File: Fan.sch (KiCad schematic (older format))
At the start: 0 parts

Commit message: Understanding the Current/Fan Driver Module
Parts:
- added Q?: MOSFET_N, symbol MOSFET_N
- added R? (x5): R, symbol R
- added RV?: POT, symbol POT
- added U?: LM324, symbol LM324
- added U?: MCP4922-E/SL, SO14, symbol MCP4922-E/SL
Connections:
- net Fan_In: now also R?.2, R?.2
- net Power+: now also Q?.S
- new net: Q?.G, U?.1
- new net: R?.2, R?.2, RV?.3, U?.3 (+)
- new net: R?.1, U?.14 (VoutA)
- new net: R?.1, U?.9 (~SHDN~)
- new net +12V: Q?.D, R?.1, U?.4 (V+)
- new net -12V: U?.11 (V-)
- new net AGND: R?.2, RV?.1
- new net CS_N: U?.3 (~CS~)
- new net Current_Measure: R?.1, U?.2 (-)
- new net MOSI: U?.5 (SDI)
- new net SCLK: U?.4 (SCK)
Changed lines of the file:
@@
 LIBS:contrib
 LIBS:valves
+LIBS:MyComponents
 LIBS:BenchBuddy-cache
 EELAYER 24 0
@@
 Comment4 ""
 $EndDescr
-Text HLabel 9250 2250 2    60   Output ~ 0
+Text HLabel 9500 2750 2    60   Output ~ 0
 Power+
-Text HLabel 9250 2550 2    60   Input ~ 0
+Text HLabel 9500 3050 2    60   Input ~ 0
 Power-
-Text HLabel 9250 2900 2    60   Input ~ 0
+Text HLabel 10250 5150 2    60   Input ~ 0
 Tach_In
-Text HLabel 1850 2050 0    60   Output ~ 0
+Text HLabel 1700 5150 0    60   Output ~ 0
 Tach_Out
-Text HLabel 1850 2350 0    60   Input ~ 0
+Text HLabel 1750 3350 0    60   Input ~ 0
 Fan_In
+Wire Wire Line
+	1700 5150 10250 5150
+$Comp
+L LM324 U?
+U 1 1 52F15AC1
+P 6750 2200
+F 0 "U?" H 6800 2400 60  0000 C CNN
+F 1 "LM324" H 6900 2000 50  0000 C CNN
+F 2 "" H 6750 2200 60  0000 C CNN
+F 3 "" H 6750 2200 60  0000 C CNN
+	1    6750 2200
+	1    0    0    -1
+$EndComp
+$Comp
+L MOSFET_N Q?
+U 1 1 52F15ADF
+P 8100 2200
+F 0 "Q?" H 8110 2370 60  0000 R CNN
+F 1 "MOSFET_N" H 8110 2050 60  0000 R CNN
+F 2 "" H 8100 2200 60  0000 C CNN
+F 3 "" H 8100 2200 60  0000 C CNN
+	1    8100 2200
+	1    0    0    -1
+$EndComp
+$Comp
+L +12V #PWR?
+U 1 1 52F15AF3
+P 8200 1750
+F 0 "#PWR?" H 8200 1700 20  0001 C CNN
+F 1 "+12V" H 8200 1850 30  0000 C CNN
+F 2 "" H 8200 1750 60  0000 C CNN
+F 3 "" H 8200 1750 60  0000 C CNN
+	1    8200 1750
+	1    0    0    -1
+$EndComp
+Wire Wire Line
+	7900 2200 7250 2200
+Wire Wire Line
+	8200 2400 8200 2750
+Wire Wire Line
+	8200 2750 9500 2750
+Wire Wire Line
+	6000 3050 9500 3050
+Wire Wire Line
+	8200 3050 8200 3850
+$Comp
+L R R?
+U 1 1 52F15B2A
+P 8200 4100
+F 0 "R?" V 8280 4100 40  0000 C CNN
+F 1 "R" V 8207 4101 40  0000 C CNN
+F 2 "" V 8130 4100 30  0000 C CNN
+F 3 "" H 8200 4100 30  0000 C CNN
+	1    8200 4100
+	1    0    0    -1
+$EndComp
+$Comp
+L AGND #PWR?
+U 1 1 52F15B46
+P 8200 4700
+F 0 "#PWR?" H 8200 4700 40  0001 C CNN
+F 1 "AGND" H 8200 4630 50  0000 C CNN
+F 2 "" H 8200 4700 60  0000 C CNN
+F 3 "" H 8200 4700 60  0000 C CNN
+	1    8200 4700
+	1    0    0    -1
+$EndComp
+Wire Wire Line
+	8200 4350 8200 4700
+Wire Wire Line
+	6000 3050 6000 2300
+Wire Wire Line
+	6000 2300 6250 2300
+Connection ~ 8200 3050
+Wire Wire Line
+	8200 2000 8200 1750
+$Comp
+L +12V #PWR?
+U 1 1 52F15B77
+P 6650 1700
+F 0 "#PWR?" H 6650 1650 20  0001 C CNN
+F 1 "+12V" H 6650 1800 30  0000 C CNN
+F 2 "" H 6650 1700 60  0000 C CNN
+F 3 "" H 6650 1700 60  0000 C CNN
+	1    6650 1700
+	1    0    0    -1
+$EndComp
+Wire Wire Line
+	6650 1700 6650 1800
+$Comp
+L -12V #PWR?
+U 1 1 52F15B91
+P 6650 2700
+F 0 "#PWR?" H 6650 2830 20  0001 C CNN
+F 1 "-12V" H 6650 2800 30  0000 C CNN
+F 2 "" H 6650 2700 60  0000 C CNN
+F 3 "" H 6650 2700 60  0000 C CNN
+	1    6650 2700
+	-1   0    0    1
+$EndComp
+Wire Wire Line
+	6650 2700 6650 2600
+$Comp
+L R R?
+U 1 1 52F15BC1
+P 5400 1700
+F 0 "R?" V 5480 1700 40  0000 C CNN
+F 1 "R" V 5407 1701 40  0000 C CNN
+F 2 "" V 5330 1700 30  0000 C CNN
+F 3 "" H 5400 1700 30  0000 C CNN
+	1    5400 1700
+	1    0    0    -1
+$EndComp
+$Comp
+L +12V #PWR?
+U 1 1 52F15BCC
+P 5400 1350
+F 0 "#PWR?" H 5400 1300 20  0001 C CNN
+F 1 "+12V" H 5400 1450 30  0000 C CNN
+F 2 "" H 5400 1350 60  0000 C CNN
+F 3 "" H 5400 1350 60  0000 C CNN
+	1    5400 1350
+	1    0    0    -1
+$EndComp
+Wire Wire Line
+	5400 1350 5400 1450
+$Comp
+L POT RV?
+U 1 1 52F15C37
+P 5400 2550
+F 0 "RV?" H 5400 2450 50  0000 C CNN
+F 1 "POT" H 5400 2550 50  0000 C CNN
+F 2 "" H 5400 2550 60  0000 C CNN
+F 3 "" H 5400 2550 60  0000 C CNN
+	1    5400 2550
+	0    -1   -1   0
+$EndComp
+$Comp
+L AGND #PWR?
+U 1 1 52F15C5C
+P 5400 3000
+F 0 "#PWR?" H 5400 3000 40  0001 C CNN
+F 1 "AGND" H 5400 2930 50  0000 C CNN
+F 2 "" H 5400 3000 60  0000 C CNN
+F 3 "" H 5400 3000 60  0000 C CNN
+	1    5400 3000
+	1    0    0    -1
+$EndComp
+Wire Wire Line
+	5400 3000 5400 2800
+Wire Wire Line
+	5400 1950 5400 2300
+Wire Wire Line
+	4300 2100 6250 2100
+Connection ~ 5400 2100
+Text HLabel 1900 1850 0    60   Output ~ 0
+MISO
+Text HLabel 1900 2050 0    60   Input ~ 0
+MOSI
+Text HLabel 1900 2150 0    60   Input ~ 0
+SCLK
+Text HLabel 1900 2250 0    60   Input ~ 0
+CS_N
+Text HLabel 1750 3700 0    60   Output ~ 0
+Current_Measure
+$Comp
+L R R?
+U 1 1 52F15DC9
+P 5700 2550
+F 0 "R?" V 5780 2550 40  0000 C CNN
+F 1 "R" V 5707 2551 40  0000 C CNN
+F 2 "" V 5630 2550 30  0000 C CNN
+F 3 "" H 5700 2550 30  0000 C CNN
+	1    5700 2550
+	1    0    0    -1
+$EndComp
+Wire Wire Line
+	1750 3700 8200 3700
+Connection ~ 8200 3700
+Wire Wire Line
+	5700 3350 5700 2800
+Wire Wire Line
+	1750 3350 5700 3350
+$Comp
+L R R?
+U 1 1 52F15E21
+P 4050 2100
+F 0 "R?" V 4130 2100 40  0000 C CNN
+F 1 "R" V 4057 2101 40  0000 C CNN
+F 2 "" V 3980 2100 30  0000 C CNN
+F 3 "" H 4050 2100 30  0000 C CNN
+	1    4050 2100
+	0    -1   -1   0
+$EndComp
+Wire Wire Line
+	1900 2050 2200 2050
+Wire Wire Line
+	1900 2150 2200 2150
+Wire Wire Line
+	1900 2250 2200 2250
+$Comp
+L R R?
+U 1 1 52F15EBA
+P 2200 2800
+F 0 "R?" V 2280 2800 40  0000 C CNN
+F 1 "R" V 2207 2801 40  0000 C CNN
+F 2 "" V 2130 2800 30  0000 C CNN
+F 3 "" H 2200 2800 30  0000 C CNN
+	1    2200 2800
+	1    0    0    -1
+$EndComp
+Wire Wire Line
+	2200 3050 2200 3350
+Connection ~ 2200 3350
+$Comp
+L MCP4922-E/SL U?
+U 1 1 52F15F05
+P 2750 2250
+F 0 "U?" H 2900 2650 40  0000 L BNN
+F 1 "MCP4922-E/SL" H 2900 2600 40  0000 L BNN
+F 2 "SO14" H 2750 2250 30  0000 C CIN
+F 3 "" H 2750 2250 60  0000 C CNN
+	1    2750 2250
+	1    0    0    -1
+$EndComp
+Wire Wire Line
+	3300 2100 3800 2100
+Wire Wire Line
+	2200 2450 2200 2550
 $EndSCHEMATC

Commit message: Understanding the Arduino Module
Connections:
- net Current_Measure renamed CURR_MEAS
- net Fan_In renamed FAN_EN_N
- net Power+ renamed FAN_OUT+
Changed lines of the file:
@@
 LIBS:valves
 LIBS:MyComponents
+LIBS:arduino_shieldsNCL
 LIBS:BenchBuddy-cache
 EELAYER 24 0
@@
 $Descr A4 11693 8268
 encoding utf-8
-Sheet 8 9
+Sheet 9 9
 Title ""
 Date ""
@@
 $EndDescr
 Text HLabel 9500 2750 2    60   Output ~ 0
-Power+
-Text HLabel 9500 3050 2    60   Input ~ 0
-Power-
+FAN_OUT+
+Text HLabel 9500 3050 2    60   Output ~ 0
+FAN_OUT-
 Text HLabel 10250 5150 2    60   Input ~ 0
-Tach_In
+TACH_IN
 Text HLabel 1700 5150 0    60   Output ~ 0
-Tach_Out
+TACH_MEAS
 Text HLabel 1750 3350 0    60   Input ~ 0
-Fan_In
+FAN_EN_N
 Wire Wire Line
 	1700 5150 10250 5150
@@
 CS_N
 Text HLabel 1750 3700 0    60   Output ~ 0
-Current_Measure
+CURR_MEAS
 $Comp
 L R R?

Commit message: Revisting the Current/Fan Module
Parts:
- removed R? (x3): R, symbol R
- removed RV?: POT, symbol POT
- added D?: DIODE, symbol DIODE
- added Q? (x2): MOSFET_N, symbol MOSFET_N
- added TH?: THERMISTOR, symbol THERMISTOR
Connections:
- net +12V: no longer Q?.D
- net AGND: now also Q?.S, Q?.S
- net CURR_MEAS: now also Q?.S, Q?.D
- net FAN_OUT+: now also D?.2 (K), TH?.2; no longer Q?.S
- net at R?.2, U?.3 (+): now also Q?.D
- new net +12C: TH?.1
- new net FAN_MODE: Q?.G
- new net FAN_OUT-: D?.1 (A), Q?.D
- new net FAN_PWM: Q?.G
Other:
- moved on the sheet: Q?, R?, U?, U?A

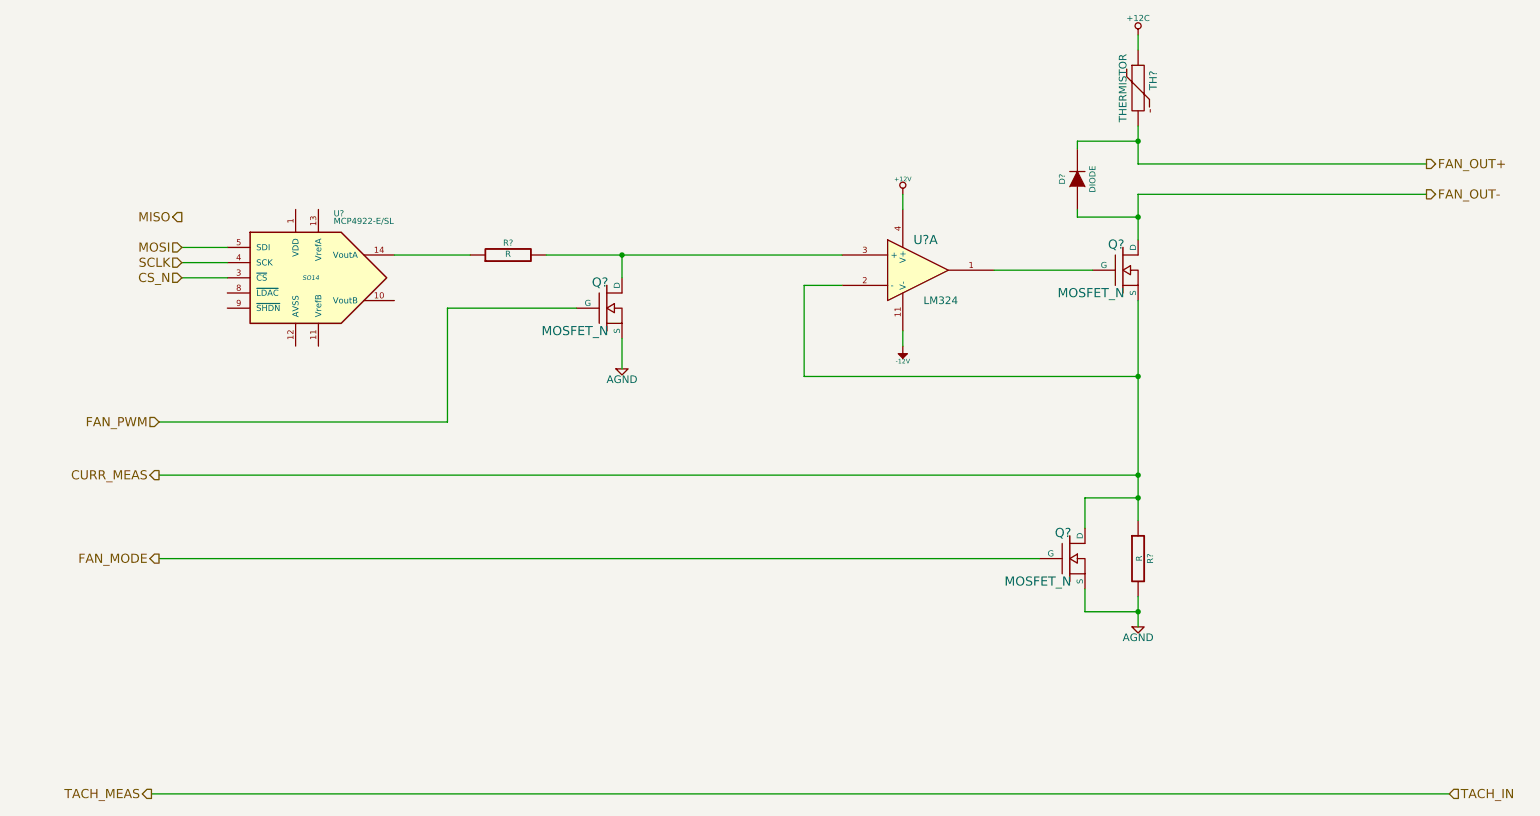
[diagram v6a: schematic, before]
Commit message: Associating and Placing the Relay Module
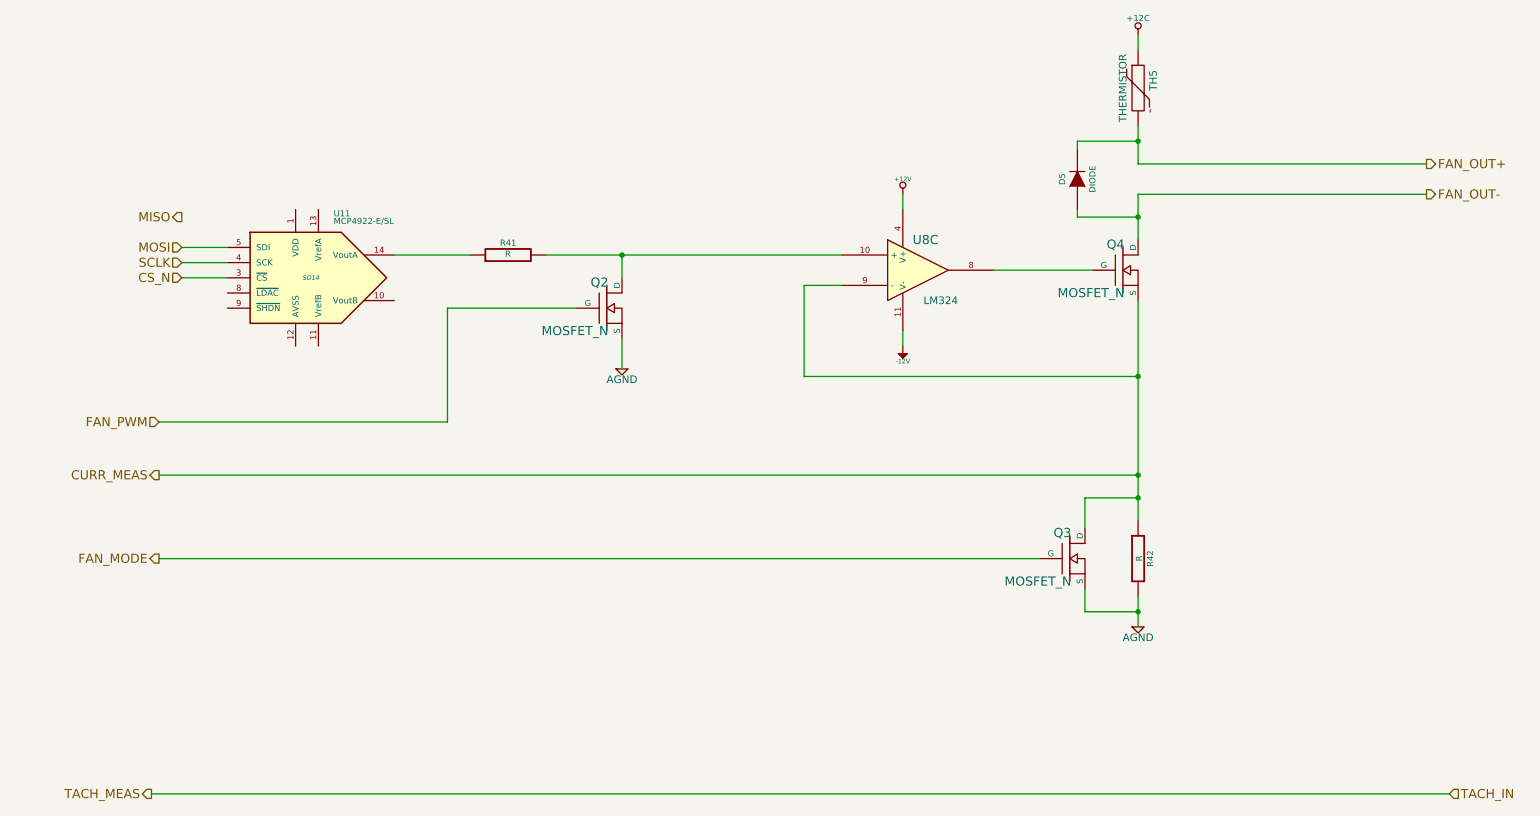
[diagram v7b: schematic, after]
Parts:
- gave numbers to parts that had none: 9
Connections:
- net CURR_MEAS: now also U8.9 (-); no longer U8.2 (-)
- net at Q4.G: now also U8.8; no longer U8.1
- net at Q2.D, R41.2: now also U8.10 (+); no longer U8.3 (+)
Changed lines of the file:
@@
 FAN_PWM
 $Comp
-L LM324 U?
-U 1 1 52F15AC1
+L LM324 U8
+U 3 1 52F15AC1
 P 6750 2350
-F 0 "U?" H 6800 2550 60  0000 C CNN
+F 0 "U8" H 6800 2550 60  0000 C CNN
 F 1 "LM324" H 6900 2150 50  0000 C CNN
 F 2 "" H 6750 2350 60  0000 C CNN
 F 3 "" H 6750 2350 60  0000 C CNN
-	1    6750 2350
-	1    0    0    -1
-$EndComp
-$Comp
-L MOSFET_N Q?
+	3    6750 2350
+	1    0    0    -1
+$EndComp
+$Comp
+L MOSFET_N Q4
 U 1 1 52F15ADF
 P 8100 2350
-F 0 "Q?" H 8110 2520 60  0000 R CNN
+F 0 "Q4" H 8110 2520 60  0000 R CNN
 F 1 "MOSFET_N" H 8110 2200 60  0000 R CNN
 F 2 "" H 8100 2350 60  0000 C CNN
@@
 $EndComp
 $Comp
-L R R?
+L R R42
 U 1 1 52F15B2A
 P 8200 4250
-F 0 "R?" V 8280 4250 40  0000 C CNN
+F 0 "R42" V 8280 4250 40  0000 C CNN
 F 1 "R" V 8207 4251 40  0000 C CNN
 F 2 "" V 8130 4250 30  0000 C CNN
@@
 $EndComp
 $Comp
-L AGND #PWR?
+L AGND #PWR051
 U 1 1 52F15B46
 P 8200 4700
-F 0 "#PWR?" H 8200 4700 40  0001 C CNN
+F 0 "#PWR051" H 8200 4700 40  0001 C CNN
 F 1 "AGND" H 8200 4630 50  0000 C CNN
 F 2 "" H 8200 4700 60  0000 C CNN
@@
 $EndComp
 $Comp
-L +12V #PWR?
+L +12V #PWR052
 U 1 1 52F15B77
 P 6650 1850
-F 0 "#PWR?" H 6650 1800 20  0001 C CNN
+F 0 "#PWR052" H 6650 1800 20  0001 C CNN
 F 1 "+12V" H 6650 1950 30  0000 C CNN
 F 2 "" H 6650 1850 60  0000 C CNN
@@
 $EndComp
 $Comp
-L -12V #PWR?
+L -12V #PWR053
 U 1 1 52F15B91
 P 6650 2850
-F 0 "#PWR?" H 6650 2980 20  0001 C CNN
+F 0 "#PWR053" H 6650 2980 20  0001 C CNN
 F 1 "-12V" H 6650 2950 30  0000 C CNN
 F 2 "" H 6650 2850 60  0000 C CNN
@@
 $EndComp
 $Comp
-L AGND #PWR?
+L AGND #PWR054
 U 1 1 52F15C5C
 P 4800 3000
-F 0 "#PWR?" H 4800 3000 40  0001 C CNN
+F 0 "#PWR054" H 4800 3000 40  0001 C CNN
 F 1 "AGND" H 4800 2930 50  0000 C CNN
 F 2 "" H 4800 3000 60  0000 C CNN
@@
 CURR_MEAS
 $Comp
-L R R?
+L R R41
 U 1 1 52F15E21
 P 4050 2250
-F 0 "R?" V 4130 2250 40  0000 C CNN
+F 0 "R41" V 4130 2250 40  0000 C CNN
 F 1 "R" V 4057 2251 40  0000 C CNN
 F 2 "" V 3980 2250 30  0000 C CNN
@@
 $EndComp
 $Comp
-L MCP4922-E/SL U?
+L MCP4922-E/SL U11
 U 1 1 52F15F05
 P 2750 2400
-F 0 "U?" H 2900 2800 40  0000 L BNN
+F 0 "U11" H 2900 2800 40  0000 L BNN
 F 1 "MCP4922-E/SL" H 2900 2750 40  0000 L BNN
 F 2 "SO14" H 2750 2400 30  0000 C CIN
@@
 $EndComp
 $Comp
-L THERMISTOR TH?
+L THERMISTOR TH5
 U 1 1 52F82F82
 P 8200 1150
-F 0 "TH?" V 8300 1200 50  0000 C CNN
+F 0 "TH5" V 8300 1200 50  0000 C CNN
 F 1 "THERMISTOR" V 8100 1150 50  0000 C CNN
 F 2 "" H 8200 1150 60  0000 C CNN
@@
 $EndComp
 $Comp
-L DIODE D?
+L DIODE D5
 U 1 1 52F8300A
 P 7800 1750
-F 0 "D?" H 7800 1850 40  0000 C CNN
+F 0 "D5" H 7800 1850 40  0000 C CNN
 F 1 "DIODE" H 7800 1650 40  0000 C CNN
 F 2 "" H 7800 1750 60  0000 C CNN
@@
 $EndComp
 $Comp
-L MOSFET_N Q?
+L MOSFET_N Q3
 U 1 1 52F830F3
 P 7750 4250
-F 0 "Q?" H 7760 4420 60  0000 R CNN
+F 0 "Q3" H 7760 4420 60  0000 R CNN
 F 1 "MOSFET_N" H 7760 4100 60  0000 R CNN
 F 2 "" H 7750 4250 60  0000 C CNN
@@
 Connection ~ 8200 3050
 $Comp
-L MOSFET_N Q?
+L MOSFET_N Q2
 U 1 1 52F83231
 P 4700 2600
-F 0 "Q?" H 4710 2770 60  0000 R CNN
+F 0 "Q2" H 4710 2770 60  0000 R CNN
 F 1 "MOSFET_N" H 4710 2450 60  0000 R CNN
 F 2 "" H 4700 2600 60  0000 C CNN
@@
 FAN_MODE
 $Comp
-L +12C #PWR?
+L +12C #PWR055
 U 1 1 52F83877
 P 8200 800
-F 0 "#PWR?" H 8200 770 30  0001 C CNN
+F 0 "#PWR055" H 8200 770 30  0001 C CNN
 F 1 "+12C" H 8200 910 40  0000 C CNN
 F 2 "" H 8200 800 60  0000 C CNN

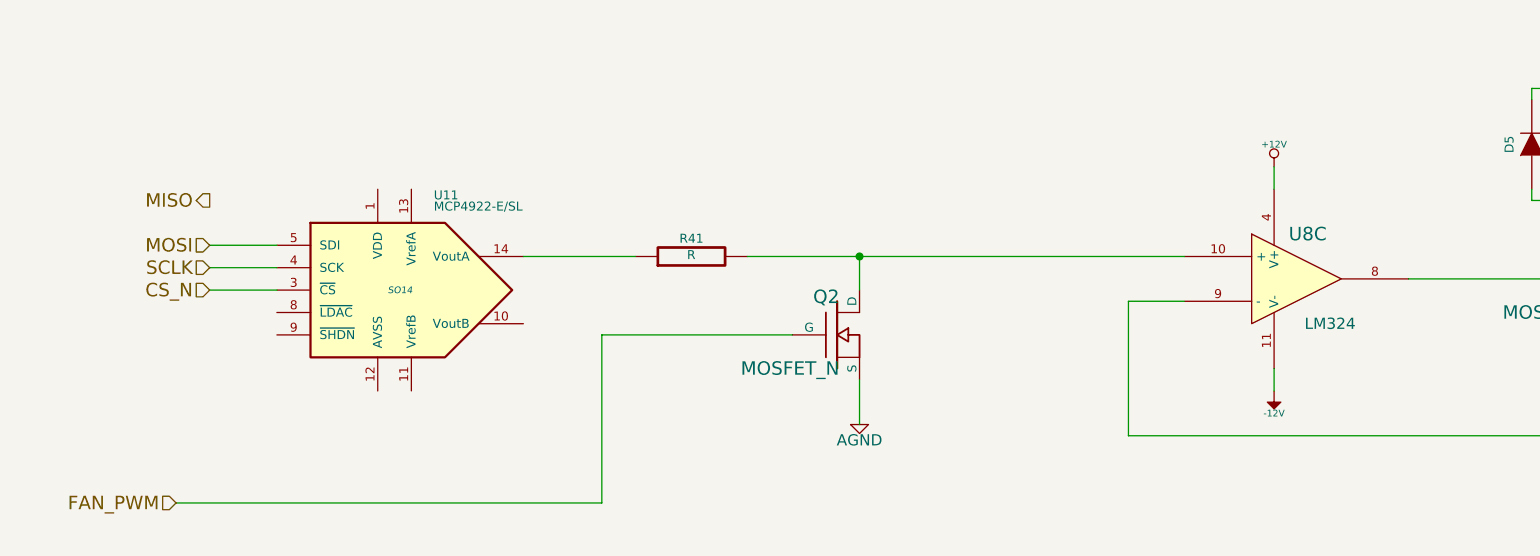
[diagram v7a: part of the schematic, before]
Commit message: Associating and Placing the Thermocouple Module
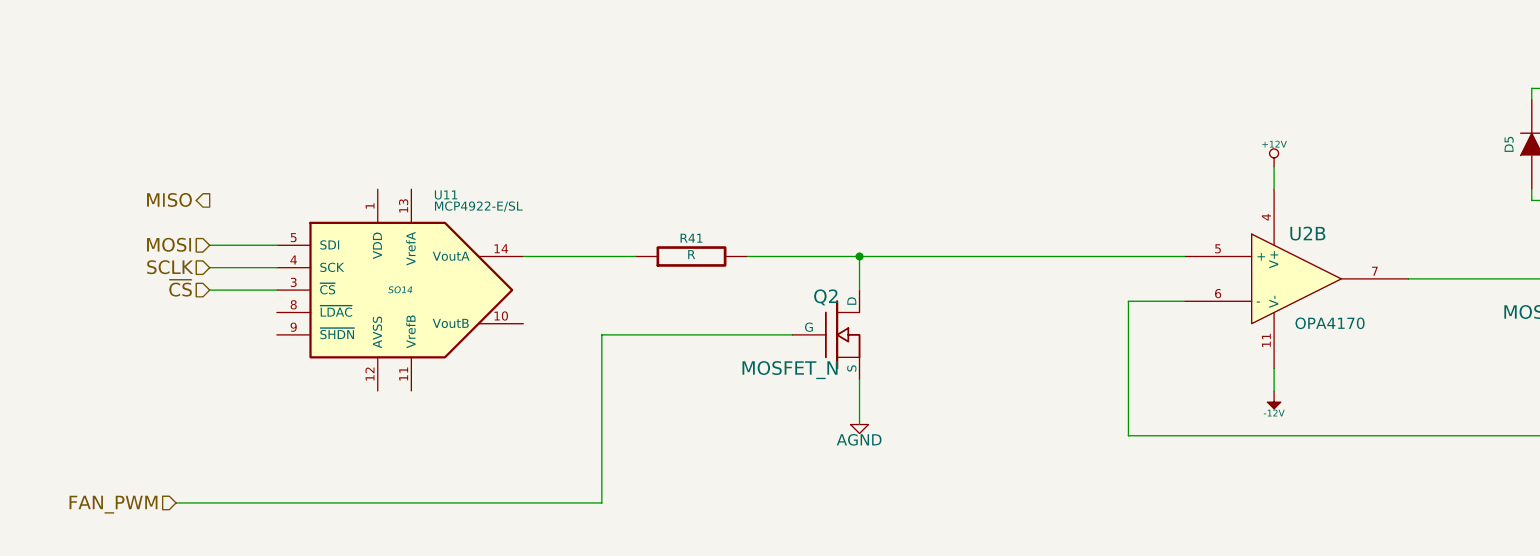
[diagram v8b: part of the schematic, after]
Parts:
- U2: renamed from U8; value LM324 -> OPA4170
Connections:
- net CURR_MEAS: now also U2.6 (-); no longer U2.9 (-)
- net at Q2.D, R41.2: now also U2.5 (+); no longer U2.10 (+)
- net at Q4.G: now also U2.7; no longer U2.8
- net CS_N renamed ~CS
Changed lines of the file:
@@
 LIBS:MyComponents
 LIBS:arduino_shieldsNCL
+LIBS:BenchBudEE
 LIBS:BenchBuddy-cache
 EELAYER 24 0
@@
 FAN_PWM
 $Comp
-L LM324 U8
-U 3 1 52F15AC1
+L LM324 U2
+U 2 1 52F15AC1
 P 6750 2350
-F 0 "U8" H 6800 2550 60  0000 C CNN
-F 1 "LM324" H 6900 2150 50  0000 C CNN
+F 0 "U2" H 6800 2550 60  0000 C CNN
+F 1 "OPA4170" H 6900 2150 50  0000 C CNN
 F 2 "" H 6750 2350 60  0000 C CNN
 F 3 "" H 6750 2350 60  0000 C CNN
-	3    6750 2350
+	2    6750 2350
 	1    0    0    -1
 $EndComp
@@
 $EndComp
 $Comp
-L AGND #PWR051
+L AGND #PWR057
 U 1 1 52F15B46
 P 8200 4700
-F 0 "#PWR051" H 8200 4700 40  0001 C CNN
+F 0 "#PWR057" H 8200 4700 40  0001 C CNN
 F 1 "AGND" H 8200 4630 50  0000 C CNN
 F 2 "" H 8200 4700 60  0000 C CNN
@@
 $EndComp
 $Comp
-L +12V #PWR052
+L +12V #PWR058
 U 1 1 52F15B77
 P 6650 1850
-F 0 "#PWR052" H 6650 1800 20  0001 C CNN
+F 0 "#PWR058" H 6650 1800 20  0001 C CNN
 F 1 "+12V" H 6650 1950 30  0000 C CNN
 F 2 "" H 6650 1850 60  0000 C CNN
@@
 $EndComp
 $Comp
-L -12V #PWR053
+L -12V #PWR059
 U 1 1 52F15B91
 P 6650 2850
-F 0 "#PWR053" H 6650 2980 20  0001 C CNN
+F 0 "#PWR059" H 6650 2980 20  0001 C CNN
 F 1 "-12V" H 6650 2950 30  0000 C CNN
 F 2 "" H 6650 2850 60  0000 C CNN
@@
 $EndComp
 $Comp
-L AGND #PWR054
+L AGND #PWR060
 U 1 1 52F15C5C
 P 4800 3000
-F 0 "#PWR054" H 4800 3000 40  0001 C CNN
+F 0 "#PWR060" H 4800 3000 40  0001 C CNN
 F 1 "AGND" H 4800 2930 50  0000 C CNN
 F 2 "" H 4800 3000 60  0000 C CNN
@@
 SCLK
 Text HLabel 1900 2400 0    60   Input ~ 0
-CS_N
+~CS
 Text HLabel 1750 3700 0    60   Output ~ 0
 CURR_MEAS
@@
 FAN_MODE
 $Comp
-L +12C #PWR055
+L +12C #PWR061
 U 1 1 52F83877
 P 8200 800
-F 0 "#PWR055" H 8200 770 30  0001 C CNN
+F 0 "#PWR061" H 8200 770 30  0001 C CNN
 F 1 "+12C" H 8200 910 40  0000 C CNN
 F 2 "" H 8200 800 60  0000 C CNN
